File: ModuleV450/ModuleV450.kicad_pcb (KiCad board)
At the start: 2 copper layers, 30 x 61.3 mm, 47 parts, among them J1 J, J2 Comms, Q1 AO3400A, U1 EL3H7(B)(TA)-G, U2 ATTINY1624-SSU-ND

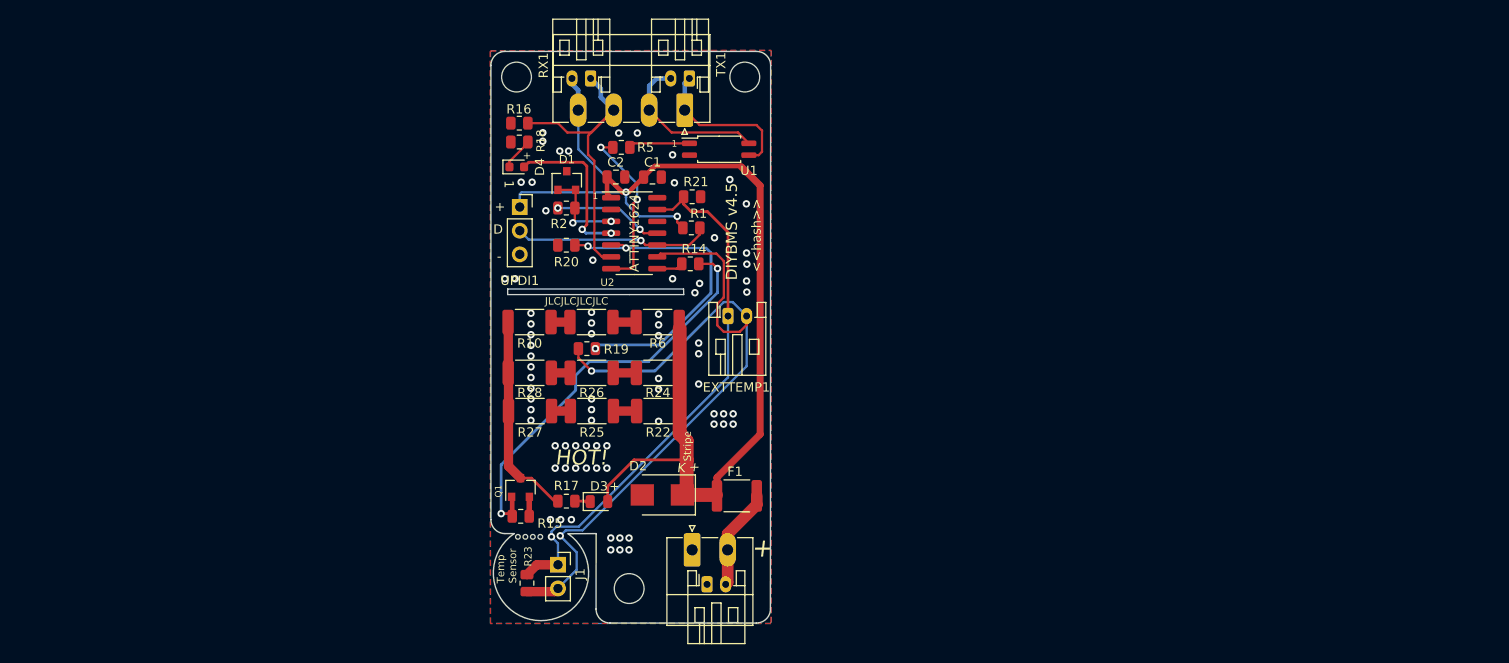
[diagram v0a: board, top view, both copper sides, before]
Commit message: prismatic diyBMS boards for LF230 / LF280 cells
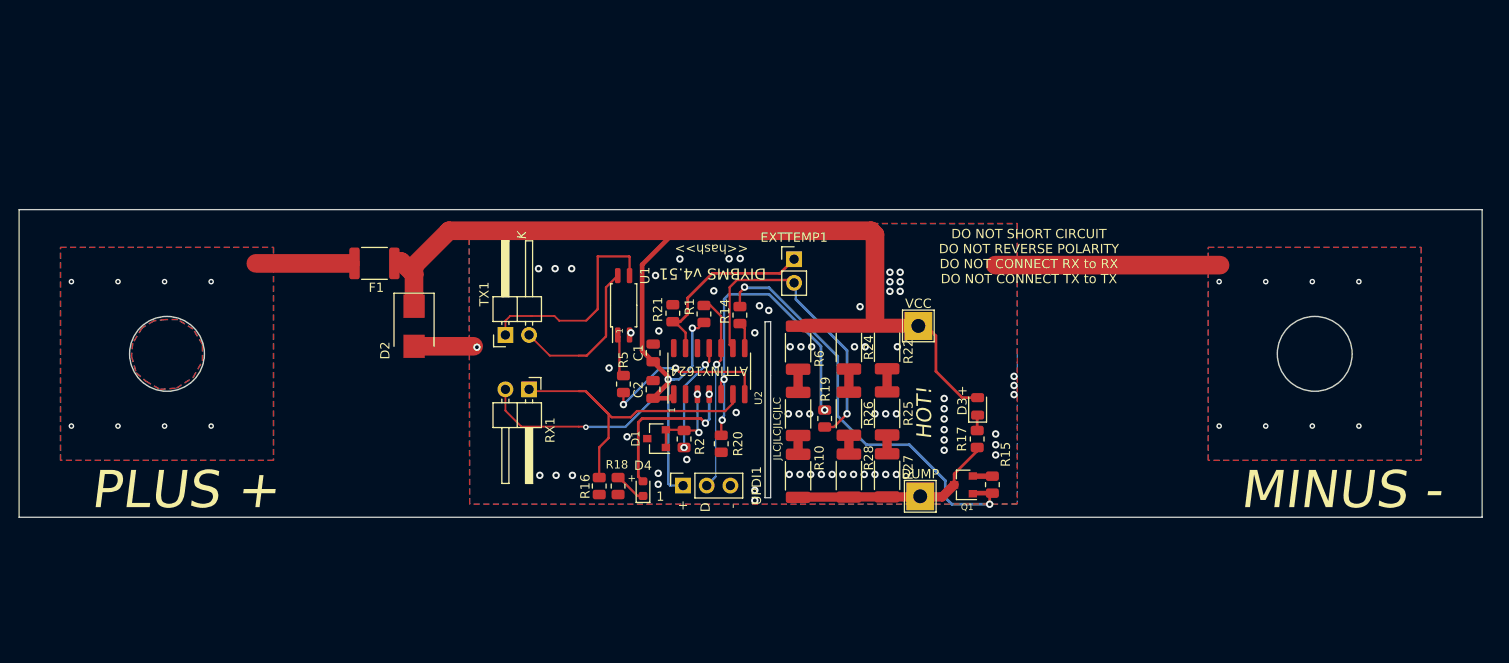
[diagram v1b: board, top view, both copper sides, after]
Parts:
- removed J1: J, Connector_PinSocket_2.54mm:PinSocket_1x02_P2.54mm_Vertical
- removed J2: Comms, Connector_Phoenix_MC:PhoenixContact_MC_1,5_4-G-3.81_1x04_P3.81mm_Horizontal
- removed POWER1: Battery, Connector_JST:JST_PH_S2B-PH-K_1x02_P2.00mm_Horizontal
- removed POWER2: Battery, Connector_Phoenix_MC:PhoenixContact_MC_1,5_2-G-3.81_1x02_P3.81mm_Horizontal
- removed R23: CMFB103F3950FANT, Resistor_SMD:R_0805_2012Metric
- removed REF** (x4): H1, Mounting_Holes:MountingHole_3.2mm_M3
- removed REF** (x3): MountingHole_3.2mm_M3, Mounting_Holes:MountingHole_3.2mm_M3
- added DUMP: TestPoint_THTPad_3.0x3.0mm_Drill1.5mm, TestPoint:TestPoint_THTPad_3.0x3.0mm_Drill1.5mm, F.Cu at (148.0, 95.7)
- added VCC: TestPoint_THTPad_3.0x3.0mm_Drill1.5mm, TestPoint:TestPoint_THTPad_3.0x3.0mm_Drill1.5mm, F.Cu at (147.8, 77.5)
- EXTTEMP1: footprint Connector_JST:JST_PH_S2B-PH-K_1x02_P2.00mm_Horizontal -> Connector_PinHeader_2.54mm:PinHeader_1x02_P2.54mm_Vertical
- R15: value 10KOHMS -> 10K
- R2: value 1KOHMS -> 1k
- RX1, TX1: footprint Connector_JST:JST_PH_S2B-PH-K_1x02_P2.00mm_Horizontal -> Connector_PinHeader_2.54mm:PinHeader_1x02_P2.54mm_Horizontal
- moved R15 50.7 mm to (155.7, 94.5), turned to 90 degrees
- moved Q1 47.6 mm to (152.6, 94.5), turned to 180 degrees
- moved F1 46.2 mm to (89.4, 70.7), turned to 180 degrees
- moved R17 44.6 mm to (154.1, 89.6), turned to 90 degrees
- moved D3 41.9 mm to (154.2, 86.1), turned to 90 degrees
- moved R16 39.9 mm to (113.5, 94.6), turned to 90 degrees
- moved R27 38.9 mm to (144.4, 93.5), turned to -90 degrees
- moved R18 38.4 mm to (115.6, 94.6), turned to 90 degrees
- moved D4 37.1 mm to (118.2, 94.9), turned to 90 degrees
- moved R28 36.0 mm to (140.3, 93.5), turned to -90 degrees
- moved UPDI1 34.7 mm to (122.5, 94.6), turned to 90 degrees
- moved RX1 34.0 mm to (106.0, 84.3), turned to -90 degrees
- moved TX1 33.9 mm to (103.5, 78.4), turned to 90 degrees
- moved R10 33.2 mm to (134.9, 93.5), turned to -90 degrees
- moved D2 32.2 mm to (93.7, 77.5), turned to -90 degrees
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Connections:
- F1 pad 2: Net-(F1-Pad2) -> unconnected-(F1-Pad2)
- U2 pad 12: (no net) -> unconnected-(U2-PA2-Pad12)
- U2 pad 2: (no net) -> unconnected-(U2-PA4-Pad2)
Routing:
- net ENABLE: track 86.4 -> 33.2 mm, vias 2 -> 1
- net PA3: track 59.3 -> 20.3 mm, vias 1 -> 0
- net VCC: track 127.5 -> 158.9 mm, vias 2 -> 3
- net GND: track 2.11 -> 32.8 mm, vias 77 -> 75
- net Net-(F1-Pad2): track 10.9 -> 0.00 mm
- net unconnected-(F1-Pad2): track 0.00 -> 10.8 mm, vias 0 -> 8
- net Net-(TX1-Pin_1): track 16.7 -> 23.5 mm
- net Net-(R5-Pad1): track 7.08 -> 4.60 mm
- net RXD0: track 33.9 -> 35.3 mm
- net Net-(Q1-G): track 45.3 -> 46.4 mm
- net REF_EN: track 12.3 -> 11.8 mm
- added copper zone on B.Cu, net unconnected-(F1-Pad2)
- added copper zone on F.Cu, net unconnected-(F1-Pad2)
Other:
- board size 30 x 61.3 mm -> 157 x 33 mm
- net class Default removed
- net class Power removed
- board text added: "DIYBMS v4.51"
- board text added: "LF230 pads should have 123mm distance"
- board text added: "MINUS -"
- board text added: "PLUS +"
- board text removed: "DIYBMS"
- board text removed: "DIYBMS v4.5"
- board text removed: "POWER"
- board text removed: "RX"
- board text removed: "Stripe"
- board text removed: "TX"
- board text removed: "Temp Sensor"
- board text removed: "github.com/stuartpittaway/diyBMSv4"
